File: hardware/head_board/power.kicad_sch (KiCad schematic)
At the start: 20 parts, among them U1 TPS54233, U2 MIC5317-3.3

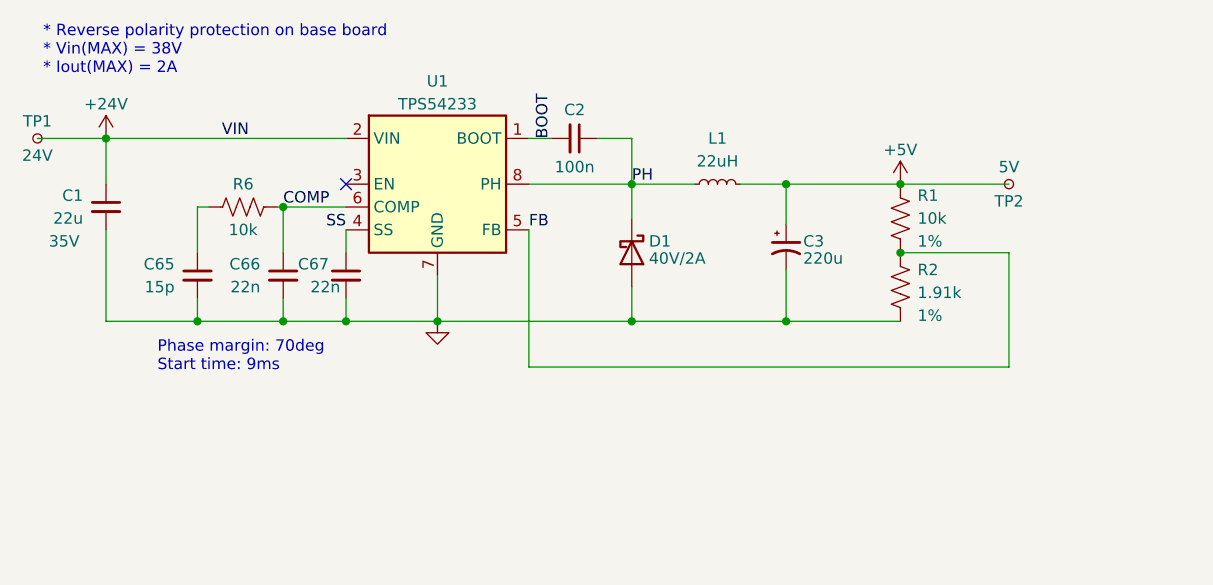
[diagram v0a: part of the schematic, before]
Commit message: Switch to power module
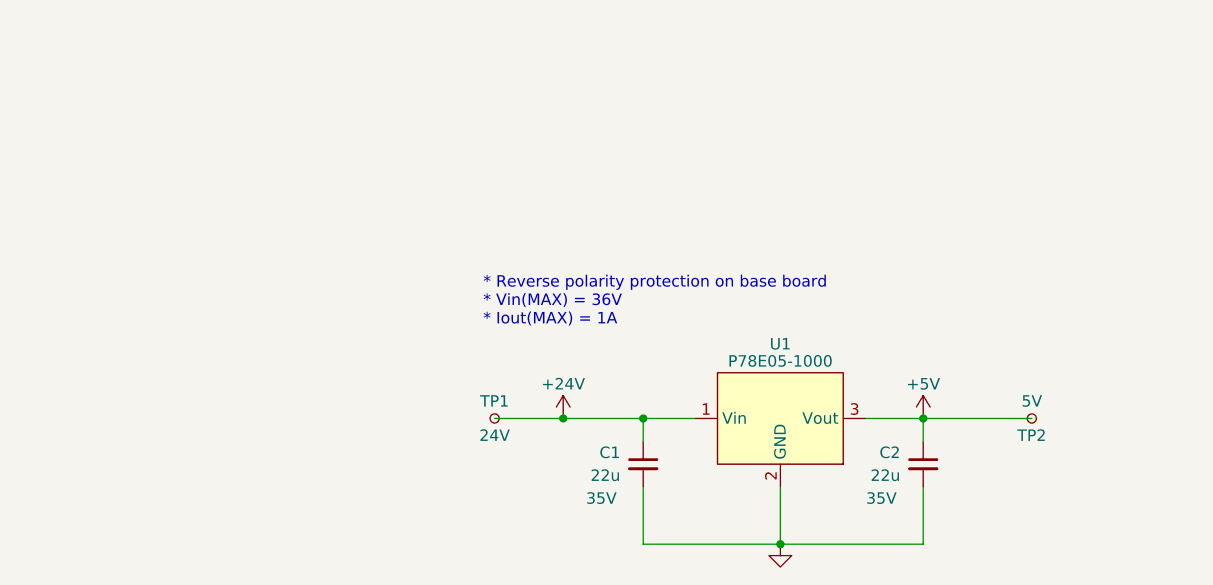
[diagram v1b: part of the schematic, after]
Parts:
- removed C3: 220u, Capacitor_SMD:CP_Elec_6.3x7.7, symbol Device:C_Polarized_Small_US
- removed C65: 15p, Capacitor_SMD:C_0402_1005Metric_Pad0.74x0.62mm_HandSolder, symbol Device:C_Small
- removed C66, C67: 22n, Capacitor_SMD:C_0603_1608Metric_Pad1.08x0.95mm_HandSolder, symbol Device:C_Small
- removed D1: 40V/2A, winterbloom:DIODE_SOD-123_SOD-123F, symbol Device:D_Schottky
- removed L1: 22uH, winterbloom:L_Murata_1255AY-220M-P3, symbol Device:L_Small
- removed R1, R6: 10k, Resistor_SMD:R_0402_1005Metric_Pad0.72x0.64mm_HandSolder, symbol Device:R_US
- removed R2: 1.91k, Resistor_SMD:R_0402_1005Metric_Pad0.72x0.64mm_HandSolder, symbol Device:R_US
- removed U1: TPS54233, Package_SO:SOIC-8_3.9x4.9mm_P1.27mm, symbol Regulator_Switching:TPS54233
- added U1: P78E05-1000, winterbloom:Converter_DCDC_CUI_P78E-1000_THT, symbol winterbloom:P78E-1000
- C2: value 100n -> 22u; footprint Capacitor_SMD:C_0603_1608Metric_Pad1.08x0.95mm_HandSolder -> Capacitor_SMD:C_0805_2012Metric_Pad1.18x1.45mm_HandSolder; Rating 50V -> 35V; mpn CL10B104KB8NNWC -> C2012X5R1V226M125AC
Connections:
- net BOOT is gone; now on net GND: C2.2
- net PH is gone; now on net +5V: C2.1
- net +24V: now also U1.1 (Vin)
- net +5V: now also U1.3 (Vout)
- net GND: now also U1.2 (GND)
- no-connect marks 1 -> 0
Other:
- note added: "* Reverse polarity protection on base board * Vin(MAX) = 36V * Iout(MAX) = 1A"
- note removed: "* Reverse polarity protection on base board * Vin(MAX) = 38V * Iout(MAX) = 2A"
- note removed: "Phase margin: 70deg Start time: 9ms"
- moved on the sheet: C1, TP1, TP2

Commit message: v1 revision to the schematic
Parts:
- removed U1: P78E05-1000, winterbloom:Converter_DCDC_CUI_P78E-1000_THT, symbol winterbloom:P78E-1000
- added C?: 22u, Capacitor_SMD:C_0805_2012Metric_Pad1.18x1.45mm_HandSolder, symbol Device:C_Small
- added C? (x2): 100n, Capacitor_SMD:C_0402_1005Metric_Pad0.74x0.62mm_HandSolder, symbol Device:C_Small
- added C?: 4.7u, Capacitor_SMD:C_0805_2012Metric_Pad1.18x1.45mm_HandSolder, symbol Device:C_Small
- added C?: 200u, symbol Device:C_Polarized_Small_US
- added D?: 5V, winterbloom:LED_0805_Kingbright_APT2012, symbol Device:LED_Filled
- added D?: 3V3, winterbloom:LED_0805_Kingbright_APT2012, symbol Device:LED_Filled
- added F?: 3A, symbol Device:Polyfuse
- added FB?: 60Ω @ 100MHz 3A, symbol Device:FerriteBead_Small
- added L? (x2): 47u, symbol Device:L_Small
- added R? (x2): 1k, Resistor_SMD:R_0603_1608Metric_Pad0.98x0.95mm_HandSolder, symbol Device:R_US
- added RV?: 35V, symbol Device:Varistor
- added TP?: GND, TestPoint:TestPoint_Pad_1.0x1.0mm, symbol Connector:TestPoint_Small
- added U1: VX7805-500, symbol winterbloom:VX7805-500
- C2: Rating 35V -> 16V
- R5: value 10k -> 4.7k
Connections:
- net +24V: now also C?.1, C?.1, C?.1, F?.2, FB?.1, FB?.2, L?.1, RV?.1; no longer C1.1
- net +3V3: now also D?.2 (A)
- net +5V: now also C?.1, D?.2 (A), L?.2; no longer C2.1
- net GND: now also C?.2, C?.2, C?.2, C?.2, C?.2, R?.2, R?.2, RV?.2, TP?.1, U1.2 (GND)
- new net: C2.1, L?.1, U1.3 (Vout)
- new net: D?.1 (K), R?.1 (x2)
- new net: C1.1, C?.1, L?.2, U1.1 (Vin)
- new net VDC: F?.1
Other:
- note added: "* Note: the base board provides reverse polarity protection"
- note added: "* Vin(MAX) = 36V * Iout(MAX) = 500mA"
- note added: "3.3V LDO"
- note added: "5V DC-DC converter"
- note added: "Fuse, MOV, & bulk capacitance"
- note added: "LEDs"
- note added: "Motor supply filter"
- note added: "Test points"
- note removed: "* Reverse polarity protection on base board * Vin(MAX) = 36V * Iout(MAX) = 1A"
- company: (none) -> Winterbloom
- title: (none) -> Candela Head
- moved on the sheet: C1, C2, C4, C5, D2, R5, TP1, TP2, TP3, U2

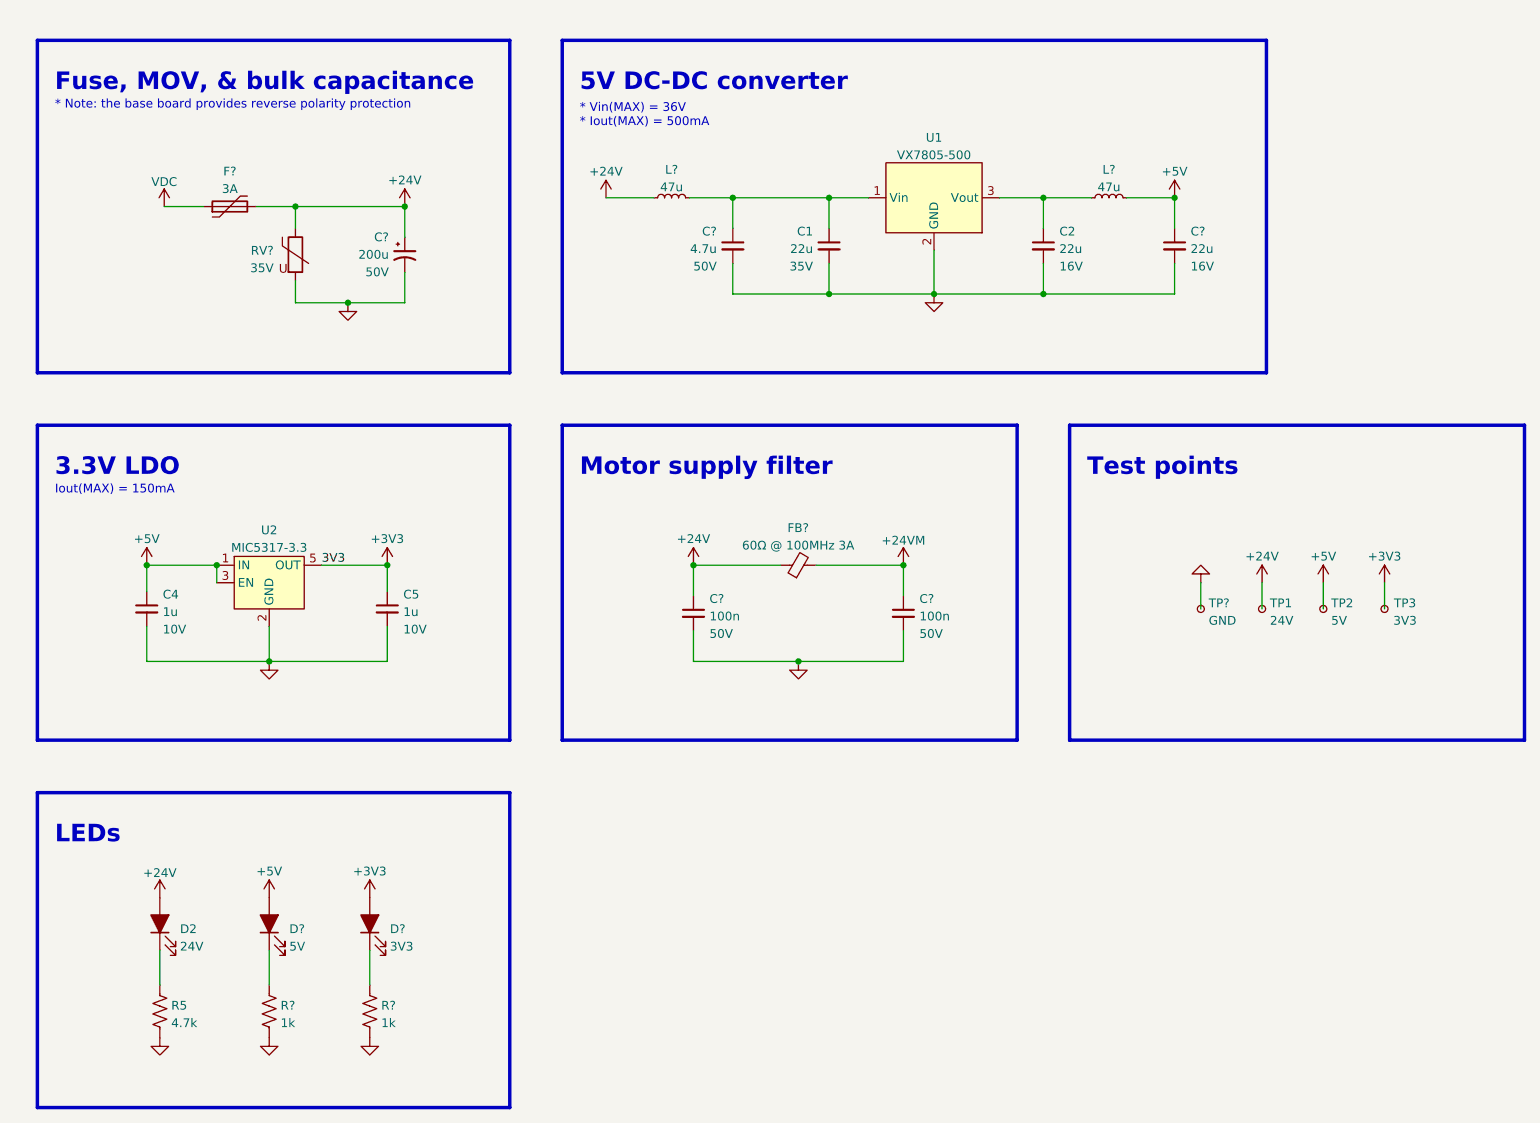
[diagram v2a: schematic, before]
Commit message: Footprints assigned
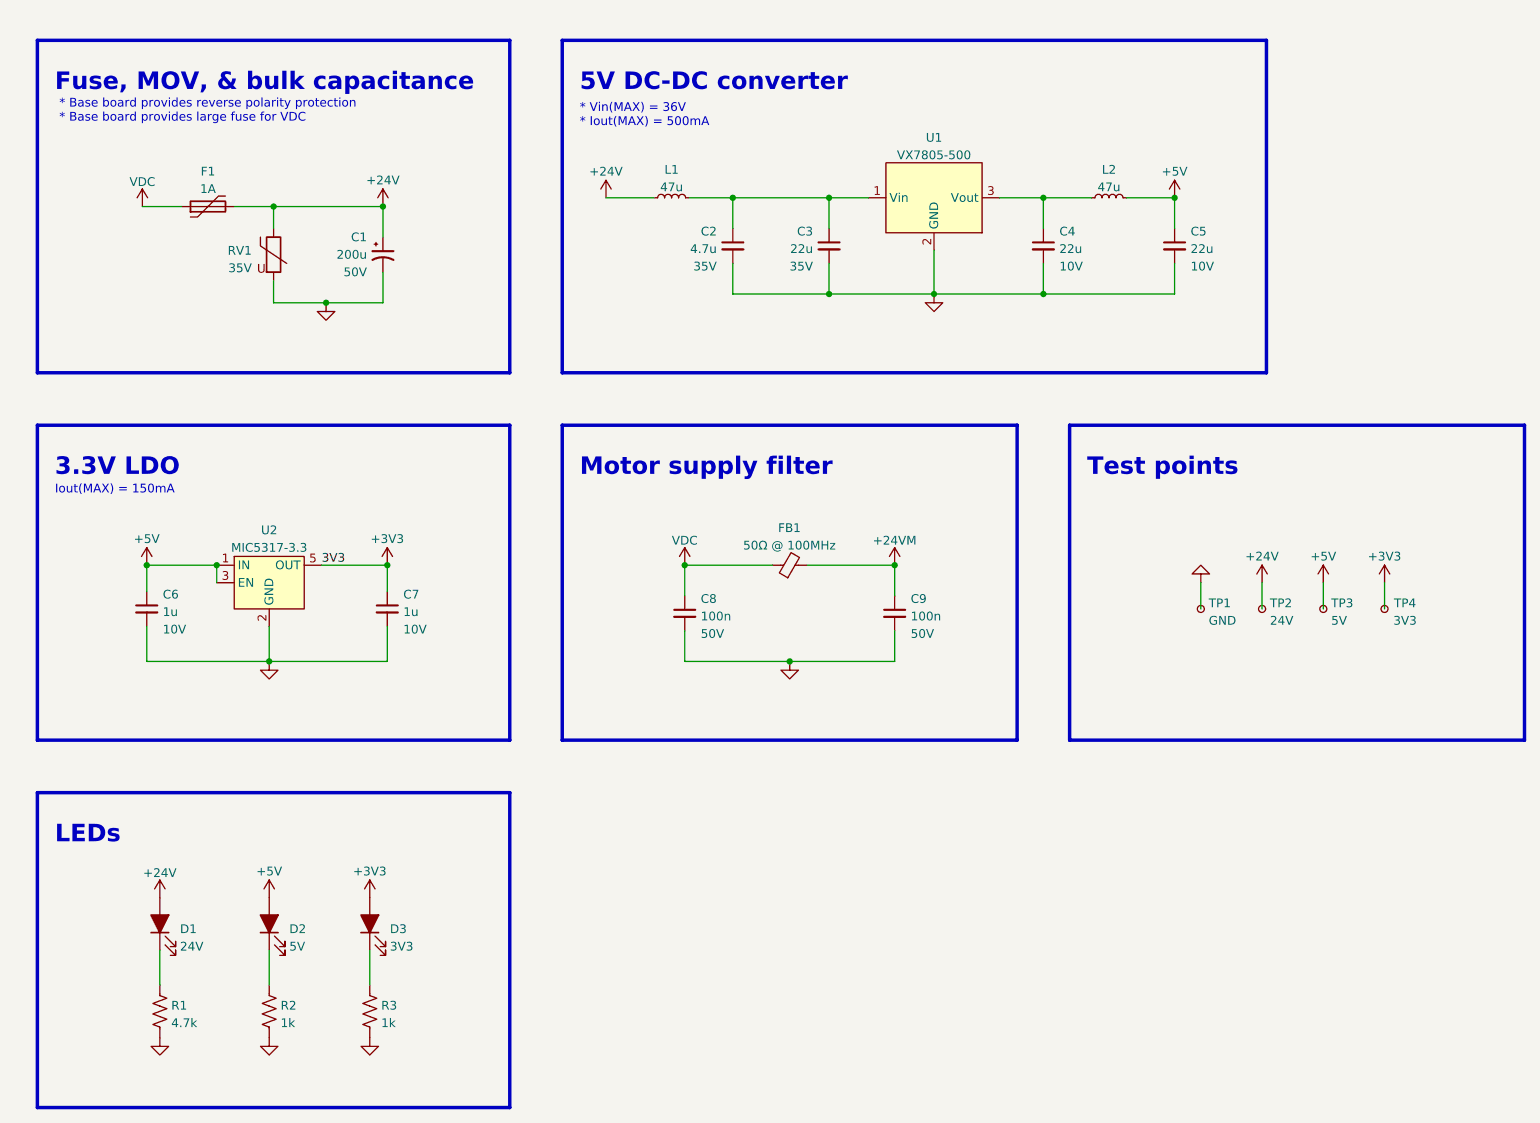
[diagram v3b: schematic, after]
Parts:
- C1: renamed from C?; footprint (none) -> Capacitor_THT:CP_Radial_D5.0mm_P2.50mm; finalized (none) -> no, footprint isn't verified
- C2: renamed from C?; Rating 50V -> 35V
- C4: renamed from C2; Rating 16V -> 10V
- C5: renamed from C?; Rating 16V -> 10V
- D1: renamed from D2; Rating (none) -> Red
- D2, D3: renamed from D?; Rating (none) -> Red
- F1: renamed from F?; value 3A -> 1A; footprint (none) -> Fuse:Fuse_1812_4532Metric_Pad1.30x3.40mm_HandSolder; mpn (none) -> 507-1773-1-ND
- FB1: renamed from FB?; value 60Ω @ 100MHz 3A -> 50Ω @ 100MHz; footprint (none) -> Inductor_SMD:L_0603_1608Metric_Pad1.05x0.95mm_HandSolder; Rating (none) -> 3A; mpn (none) -> BLM18KG121TN1D
- L1, L2: renamed from L?; footprint (none) -> Inductor_SMD:L_1210_3225Metric_Pad1.42x2.65mm_HandSolder; Rating (none) -> 500mA; mpn (none) -> VLS6045EX-470M
- R1: renamed from R5; Rating (none) -> 200mW
- R2, R3: renamed from R?; Rating (none) -> 200mW
- RV1: renamed from RV?; footprint (none) -> Resistor_SMD:R_0603_1608Metric_Pad0.98x0.95mm_HandSolder; mpn (none) -> B72500D0300H060
- U1: footprint (none) -> winterbloom:Converter_DCDC_CUI_VX78-500_THT
- gave numbers to parts that had none: 3
- renumbered C1 to C3, C4 to C6, C5 to C7, TP1 to TP2, TP2 to TP3, TP3 to TP4
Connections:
- net +24V: no longer C8.1, FB1.1
- net VDC: now also C8.1, FB1.1
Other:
- note added: "* Base board provides reverse polarity protection * Base board provides large fuse for VDC"
- note removed: "* Note: the base board provides reverse polarity protection"
- moved on the sheet: C1, C8, C9, F1, FB1, RV1

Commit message: Finish up layout for v1, ended up removing some stuff
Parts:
- removed C1: 200u, Capacitor_THT:CP_Radial_D5.0mm_P2.50mm, symbol Device:C_Polarized_Small_US
- removed C5: 22u, Capacitor_SMD:C_0805_2012Metric_Pad1.18x1.45mm_HandSolder, symbol Device:C_Small
- removed D1: 24V, winterbloom:LED_0805_Kingbright_APT2012, symbol Device:LED_Filled
- removed D2: 5V, winterbloom:LED_0805_Kingbright_APT2012, symbol Device:LED_Filled
- removed D3: 3V3, winterbloom:LED_0805_Kingbright_APT2012, symbol Device:LED_Filled
- removed F1: 1A, Fuse:Fuse_1812_4532Metric_Pad1.30x3.40mm_HandSolder, symbol Device:Polyfuse
- removed L1, L2: 47u, Inductor_SMD:L_1210_3225Metric_Pad1.42x2.65mm_HandSolder, symbol Device:L_Small
- removed R1: 4.7k, Resistor_SMD:R_0603_1608Metric_Pad0.98x0.95mm_HandSolder, symbol Device:R_US
- removed R2, R3: 1k, Resistor_SMD:R_0603_1608Metric_Pad0.98x0.95mm_HandSolder, symbol Device:R_US
- added C5: 100u, Capacitor_SMD:CP_Elec_6.3x7.7, symbol Device:C_Polarized_Small_US
- added FB14: 50Ω @ 100MHz, Inductor_SMD:L_0603_1608Metric_Pad1.05x0.95mm_HandSolder, symbol Device:FerriteBead_Small
- C2: mpn C2012X5R1V226M125AC -> ?
- C8, C9: mpn CL05A105KO5NNNC -> CL05A104KA5NNNC
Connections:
- net VDC is gone; now on net +24V: C8.1, FB1.1
- net +24V: now also FB14.1; no longer C9.1, FB1.2
- net +5V: now also C4.1, U1.3 (Vout)
- net GND: now also C5.2
- net at C2.1, C3.1, U1.1 (Vin): now also FB14.2
- new net VMOTOR: C5.1, C9.1, FB1.2
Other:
- note added: "MOV, & bulk capacitance"
- note removed: "Fuse, MOV, & bulk capacitance"
- note removed: "LEDs"
- moved on the sheet: C2, C3, C4, C8, C9, FB1, RV1, U1

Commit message: V2 of the head board (Jellyfish)
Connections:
- net VIN_FILTERED: now reaches C2.1, C3.1, FB14.2, U1.1 (Vin)
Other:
- title: Candela Head -> Jellyfish
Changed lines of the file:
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@@
   (paper "USLetter")
   (title_block
-    (title "Candela Head")
-    (date "2022-07-27")
-    (rev "v1")
+    (title "Jellyfish")
+    (date "2022-09-07")
+    (rev "v2")
     (company "Winterbloom")
     (comment 1 "Alethea Flowers")
     (comment 2 "CERN-OHL-P V2")
+    (comment 3 "jellyfish.wntr.dev")
   )
   (junction (at 107.95 43.815) (diameter 0) (color 0 0 0 0)
@@
     (effects (font (size 1.27 1.27)) (justify left bottom))
   )
+  (label "VIN_FILTERED" (at 131.445 43.815 0)
+    (effects (font (size 0.64 0.64)) (justify left bottom))
+  )
   (global_label "VMOTOR" (shape input) (at 146.05 95.885 0) (fields_autoplaced)
